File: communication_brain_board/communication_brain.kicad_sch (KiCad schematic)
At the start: 41 parts

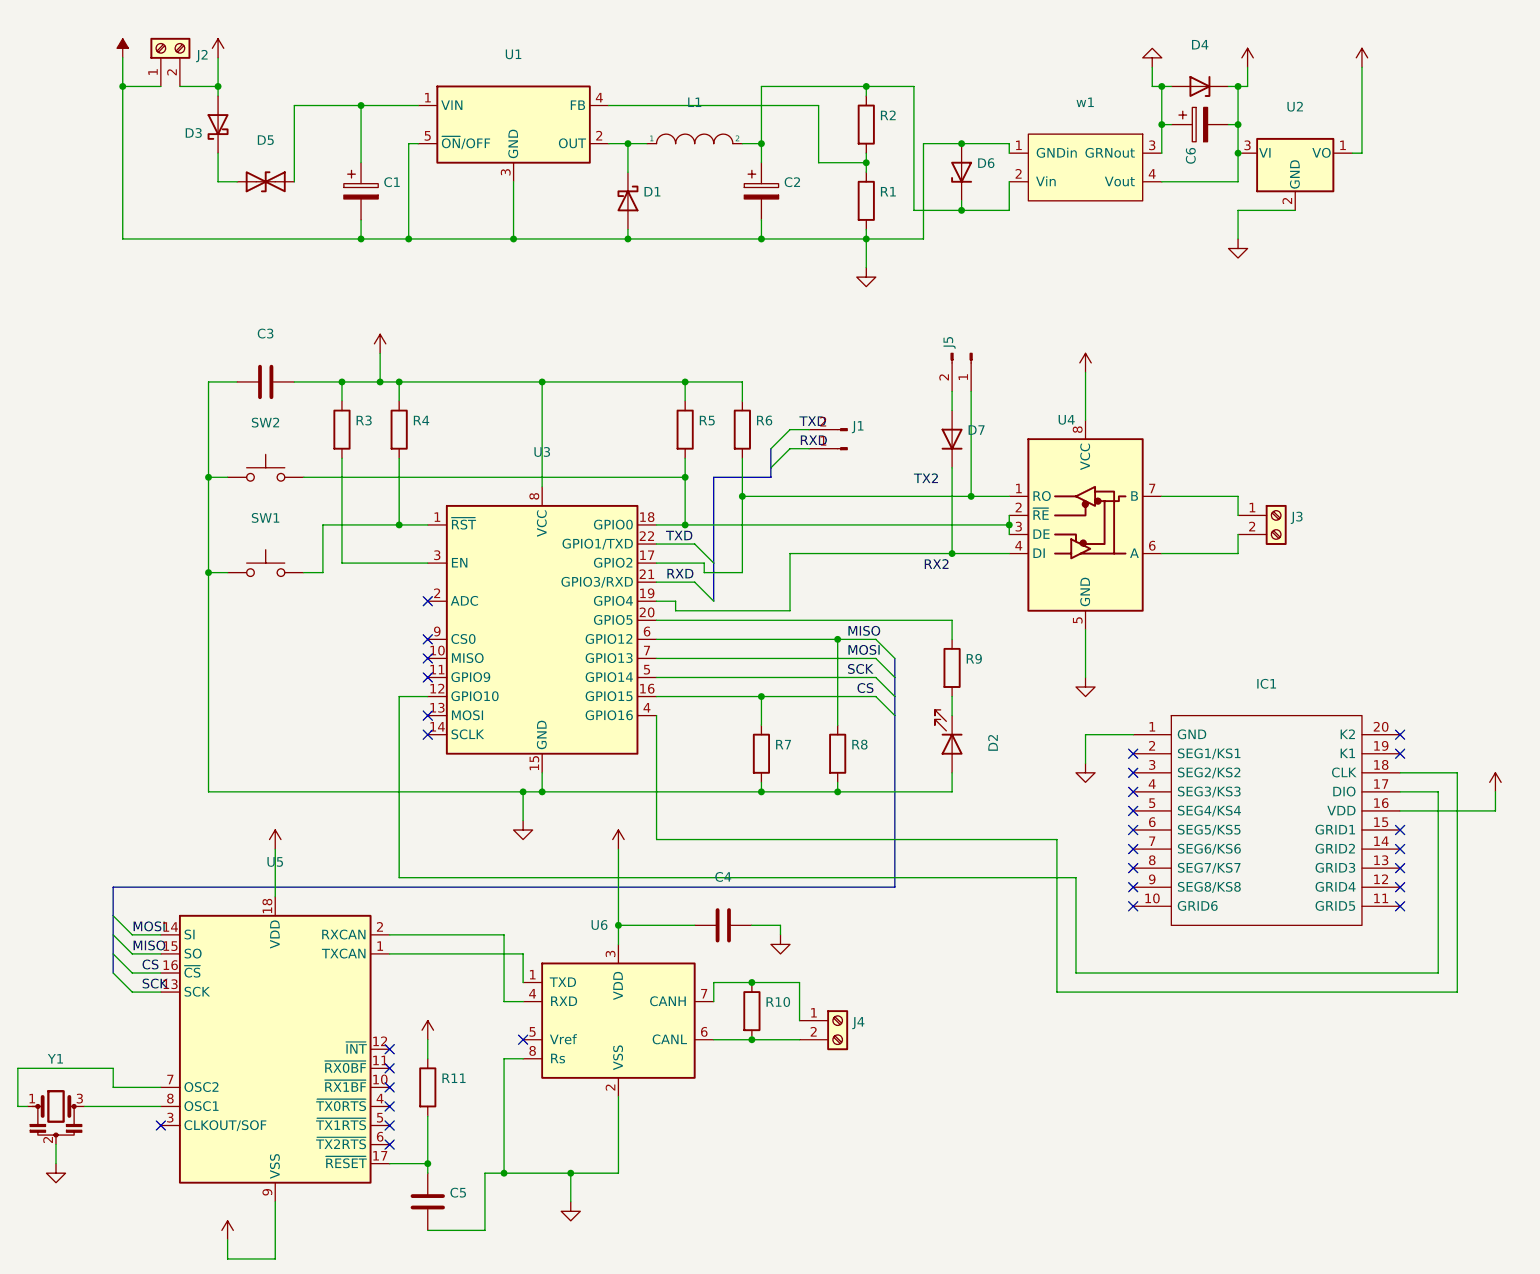
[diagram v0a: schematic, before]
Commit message: reworked to use Jiкоng bms, reworked work with spi-can library, reworked http server, smal fixes
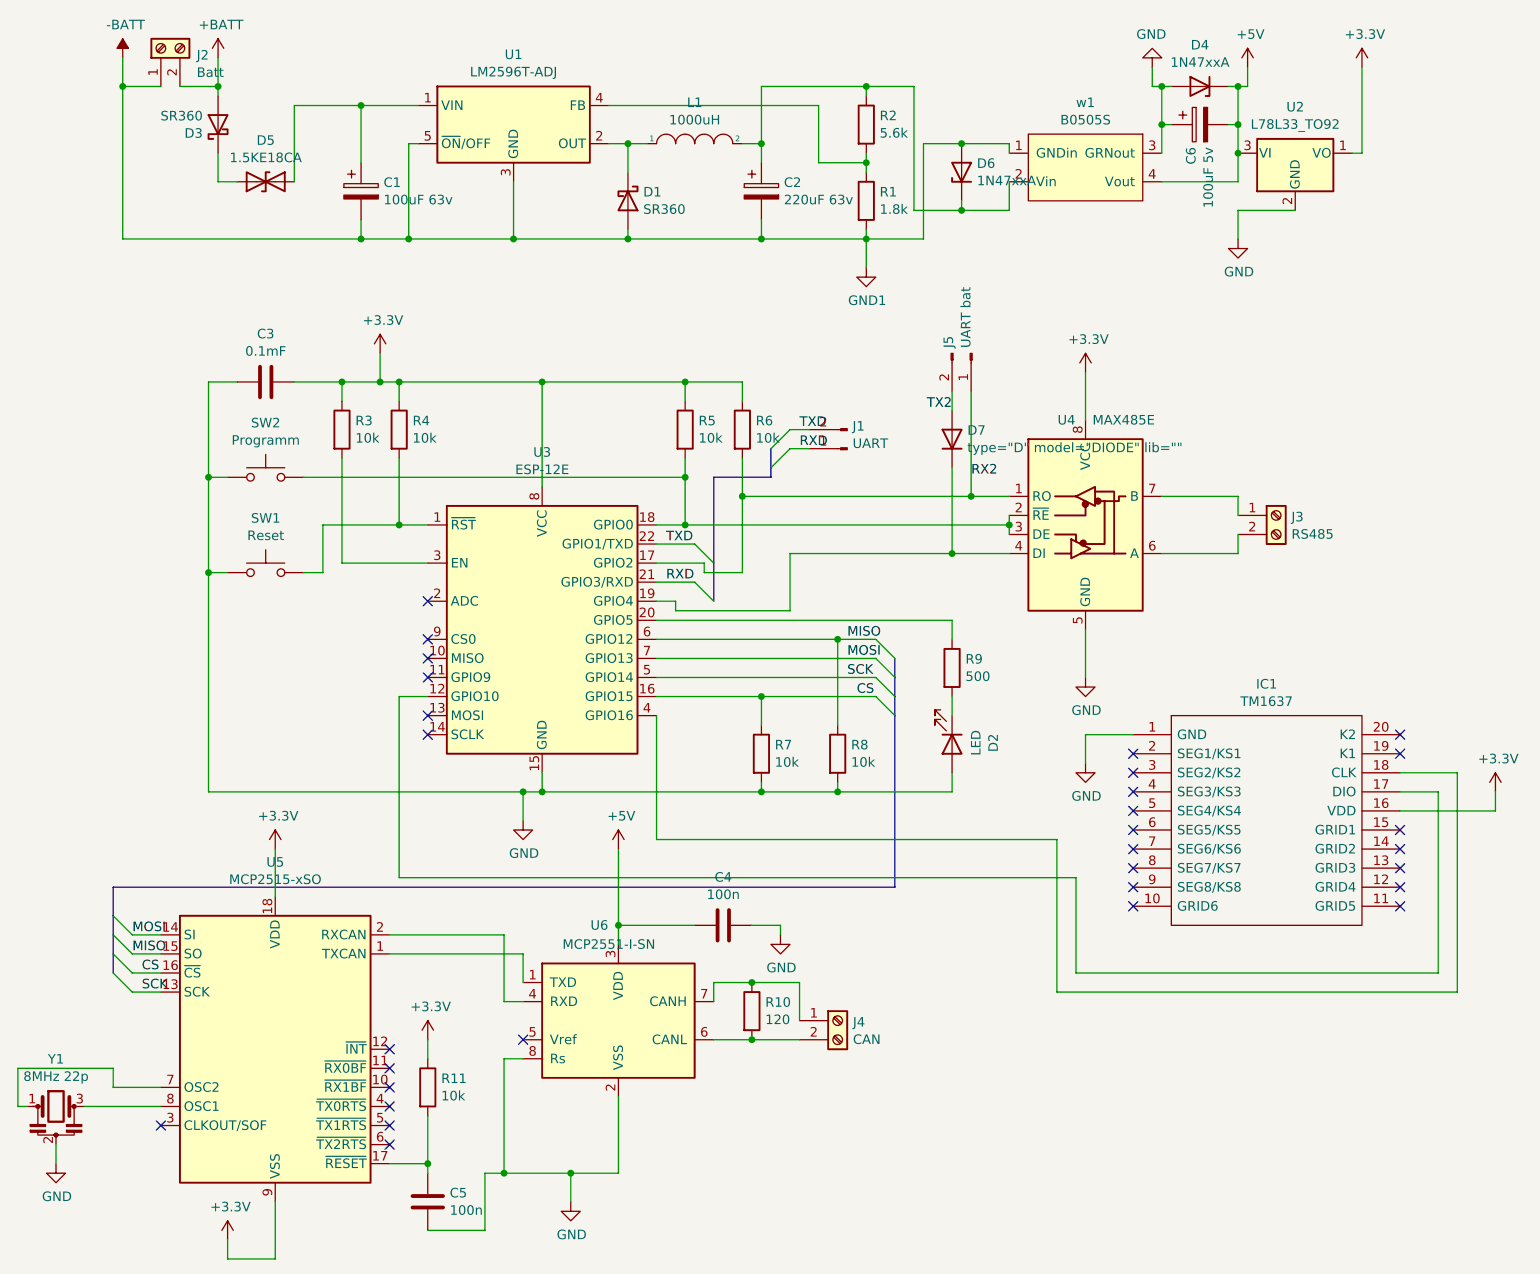
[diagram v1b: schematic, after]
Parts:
- C1: value (none) -> 100uF 63v; footprint (none) -> Capacitor_THT:C_Radial_D5.0mm_H5.0mm_P2.00mm
- C2: value (none) -> 220uF 63v; footprint (none) -> Capacitor_THT:C_Radial_D5.0mm_H5.0mm_P2.00mm
- C3: value (none) -> 0.1mF; footprint (none) -> Capacitor_THT:C_Disc_D7.5mm_W5.0mm_P5.00mm
- C4, C5: value (none) -> 100n
- C6: value (none) -> 100uF 5v; footprint (none) -> Capacitor_THT:C_Radial_D5.0mm_H5.0mm_P2.00mm
- D1, D3: value (none) -> SR360; footprint (none) -> Diode_THT:D_DO-201AD_P15.24mm_Horizontal
- D2: value (none) -> LED
- D4, D6: value (none) -> 1N47xxA; footprint (none) -> Diode_THT:D_DO-41_SOD81_P10.16mm_Horizontal
- D5: value (none) -> 1.5KE18CA; footprint (none) -> Diode_THT:D_DO-201AE_P15.24mm_Horizontal
- D7: value (none) -> ${SIM.PARAMS}; Spice_Netlist_Enabled Y -> (none); Spice_Primitive D -> (none)
- IC1: value (none) -> TM1637; footprint (none) -> DIP778W53P254L2612H431Q20N
- J1: value (none) -> UART; footprint (none) -> Connector_PinHeader_2.00mm:PinHeader_1x02_P2.00mm_Vertical
- J2: value (none) -> Batt; footprint (none) -> TerminalBlock_4Ucon:TerminalBlock_4Ucon_1x02_P3.50mm_Horizontal
- J3: value (none) -> RS485; footprint (none) -> TerminalBlock_4Ucon:TerminalBlock_4Ucon_1x02_P3.50mm_Horizontal
- J4: value (none) -> CAN; footprint (none) -> TerminalBlock_4Ucon:TerminalBlock_4Ucon_1x02_P3.50mm_Horizontal
- J5: value (none) -> UART bat; footprint (none) -> Connector_PinHeader_2.00mm:PinHeader_1x02_P2.00mm_Vertical
- L1: value (none) -> 1000uH; footprint (none) -> Inductor_THT:Choke_Schaffner_RN202-04-8.8x18.2mm
- R1: value (none) -> 1.8k; footprint (none) -> Resistor_THT:R_Axial_DIN0207_L6.3mm_D2.5mm_P10.16mm_Horizontal
- R10: value (none) -> 120; footprint (none) -> Resistor_SMD:R_2010_5025Metric
- R11: value (none) -> 10k; footprint (none) -> Resistor_SMD:R_2010_5025Metric
- R2: value (none) -> 5.6k; footprint (none) -> Resistor_THT:R_Axial_DIN0207_L6.3mm_D2.5mm_P10.16mm_Horizontal
- R3, R4, R5, R6, R7, R8: value (none) -> 10k; footprint (none) -> Resistor_THT:R_Axial_DIN0207_L6.3mm_D2.5mm_P10.16mm_Horizontal
- R9: value (none) -> 500; footprint (none) -> Resistor_THT:R_Axial_DIN0207_L6.3mm_D2.5mm_P10.16mm_Horizontal
- SW1: value (none) -> Reset; footprint (none) -> Button_Switch_THT:SW_PUSH_6mm_H5mm
- SW2: value (none) -> Programm; footprint (none) -> Button_Switch_THT:SW_PUSH_6mm_H5mm
- U1: value (none) -> LM2596T-ADJ; footprint (none) -> Package_TO_SOT_THT:TO-220-5_P3.4x3.7mm_StaggerOdd_Lead3.8mm_Vertical
- U2: value (none) -> L78L33_TO92; footprint (none) -> Package_TO_SOT_THT:TO-92_Inline
- U3: value (none) -> ESP-12E; footprint (none) -> RF_Module:ESP-12E
- U4: value (none) -> MAX485E; footprint (none) -> Package_SO:SOIC-8_5.23x5.23mm_P1.27mm
- U5: value (none) -> MCP2515-xSO; footprint (none) -> Package_SO:SOIC-18W_7.5x11.6mm_P1.27mm
- U6: value (none) -> MCP2551-I-SN; footprint (none) -> Package_SO:SOIC-8_3.9x4.9mm_P1.27mm
- Y1: value (none) -> 8MHz 22p
- w1: value (none) -> B0505S
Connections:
- net RX2: now also J5.1 (Pin_1), R6.2, U3.17 (GPIO2), U4.1 (RO)
- net TX2: now also D7.1 (A), J5.2 (Pin_2)
